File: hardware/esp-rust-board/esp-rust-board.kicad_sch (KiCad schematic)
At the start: 55 parts, among them J1 USB4105-GF-A, Q1 DMG3415U, SW1 SW_Push, SW2 SW_Push, U1 SHTC3, U2 ICM-42670-P, U3 ESP32-C3-MINI-1, U4 Rust_Board, U5 SY8088, U6 MCP73831T-2ACI/OT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

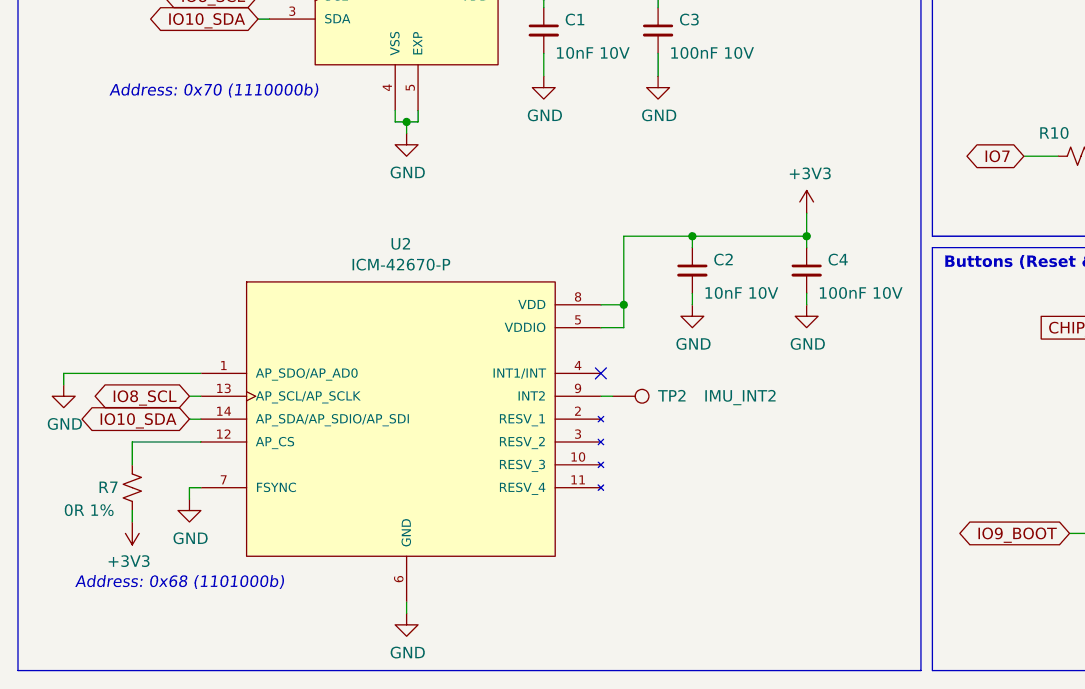
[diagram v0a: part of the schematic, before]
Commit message: Added LIS3DH
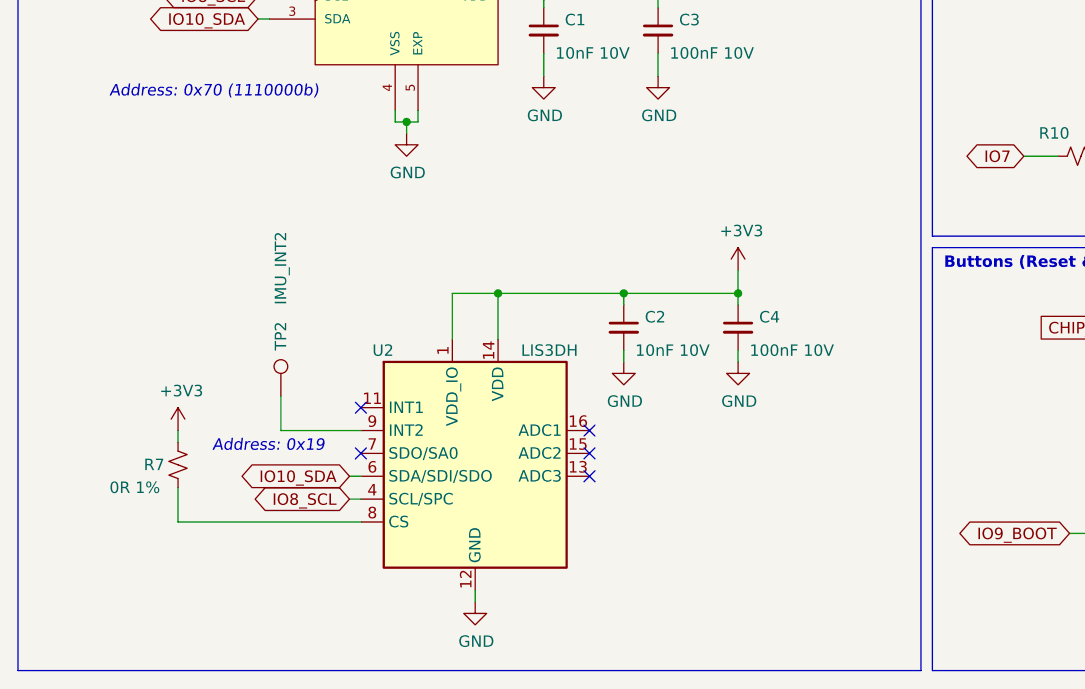
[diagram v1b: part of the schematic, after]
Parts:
- removed U2: ICM-42670-P, Rust_Board:IC_ICM-42670-P, symbol Rust_Board:ICM-42670-P
- added U2: LIS3DH, Package_LGA:LGA-16_3x3mm_P0.5mm_LayoutBorder3x5y, symbol Sensor_Motion:LIS3DH
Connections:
- net +3V3: now also R7.1, U2.1 (VDD_IO), U2.14 (VDD); no longer R7.2
- net GND: now also U2.10 (GND), U2.12 (GND), U2.5 (GND)
- net IO10_SDA: now also U2.6 (SDA/SDI/SDO)
- net IO8_SCL: now also U2.4 (SCL/SPC)
- net at TP2.1: now also U2.9 (INT2)
- new net: R7.2, U2.8 (CS)
- no-connect marks 9 -> 13
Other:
- note added: "Address: 0x19"
- note removed: "Address: 0x68 (1101000b)"
- moved on the sheet: C2, C4, R7, TP2

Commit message: Sync
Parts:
- removed TP2: IMU_INT2, TestPoint:TestPoint_Pad_D1.0mm, symbol Connector:TestPoint
- U2: LCSC (none) -> C15134
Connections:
- net +3V3: now also U2.7 (SDO/SA0)
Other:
- note added: "Address: 0x19 (0011001b)"
- note removed: "Address: 0x19"
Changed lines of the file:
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@@
   (title_block
     (title "ESP32-C3-DevKit-RUST-1")
-    (date "2022-04-27")
-    (rev "1.2a")
+    (date "2022-06-01")
+    (rev "1.2b")
     (company "Espressif")
     (comment 1 "ESP32-C3 Development Board for Rust")
+    (comment 2 "Special Version for EW22")
   )
   (junction (at 180.34 82.55) (diameter 0) (color 0 0 0 0)
@@
   )
   (no_connect (at 152.4 118.11))
+  (no_connect (at 50.8 170.18))
   (no_connect (at 231.14 81.28))
   (no_connect (at 237.49 147.32))
   (no_connect (at 237.49 139.7))
-  (no_connect (at 50.8 172.72))
   (no_connect (at 50.8 167.64))
   (no_connect (at 76.2 172.72))
@@
     (stroke (width 0) (type default) (color 0 0 0 0))
   )
-  (wire (pts (xy 41.91 170.18) (xy 50.8 170.18))
-    (stroke (width 0) (type default) (color 0 0 0 0))
-  )
   (wire (pts (xy 140.97 22.86) (xy 140.97 25.4))
     (stroke (width 0) (type default) (color 0 0 0 0))
@@
     (stroke (width 0) (type default) (color 0 0 0 0))
   )
+  (wire (pts (xy 41.91 170.18) (xy 41.91 172.72))
+    (stroke (width 0) (type default) (color 0 0 0 0))
+  )
   (wire (pts (xy 193.04 154.94) (xy 194.31 154.94))
     (stroke (width 0) (type default) (color 0 0 0 0))
@@
     (stroke (width 0) (type default) (color 0 0 0 0))
   )
-  (wire (pts (xy 41.91 166.37) (xy 41.91 170.18))
-    (stroke (width 0) (type default) (color 0 0 0 0))
-  )
   (wire (pts (xy 231.14 69.85) (xy 232.41 69.85))
     (stroke (width 0) (type default) (color 0 0 0 0))
@@
     (stroke (width 0) (type default) (color 0 0 0 0))
   )
+  (wire (pts (xy 41.91 172.72) (xy 50.8 172.72))
+    (stroke (width 0) (type default) (color 0 0 0 0))
+  )
   (wire (pts (xy 232.41 101.6) (xy 232.41 102.87))
     (stroke (width 0) (type default) (color 0 0 0 0))
@@
     (effects (font (size 1.27 1.27) (thickness 0.254) bold) (justify left bottom))
   )
-  (text "Address: 0x19" (at 34.29 172.72 0)
+  (text "Address: 0x19 (0011001b)" (at 22.86 186.69 0)
     (effects (font (size 1.27 1.27) italic) (justify left bottom))
   )
@@
     (pin "1")
   )
-  (symbol (lib_id "Connector:TestPoint") (at 41.91 166.37 0) (unit 1)
-    (in_bom no) (on_board yes)
-    (property "Reference" "TP2" (id 0) (at 41.91 161.29 90)
-      (effects (font (size 1.27 1.27)) (justify left))
-    )
-    (property "Value" "IMU_INT2" (id 1) (at 41.91 156.21 90)
-      (effects (font (size 1.27 1.27)) (justify left))
-    )
-    (property "Footprint" "TestPoint:TestPoint_Pad_D1.0mm" (id 2) (at 46.99 166.37 0)
-      (effects (font (size 1.27 1.27)) hide)
-    )
-    (property "Datasheet" "~" (id 3) (at 46.99 166.37 0)
-      (effects (font (size 1.27 1.27)) hide)
-    )
-    (pin "1")
-  )
   (symbol (lib_id "Device:C_Small") (at 80.01 158.75 0) (unit 1)
     (in_bom yes) (on_board yes)
@@
     (pin "1")
   )
+  (symbol (lib_id "power:+3V3") (at 41.91 170.18 0) (unit 1)
+    (in_bom yes) (on_board yes)
+    (property "Reference" "#PWR0112" (id 0) (at 41.91 173.99 0)
+      (effects (font (size 1.27 1.27)) hide)
+    )
+    (property "Value" "+3V3" (id 1) (at 42.291 165.7858 0))
+    (property "Footprint" "" (id 2) (at 41.91 170.18 0)
+      (effects (font (size 1.27 1.27)) hide)
+    )
+    (property "Datasheet" "" (id 3) (at 41.91 170.18 0)
+      (effects (font (size 1.27 1.27)) hide)
+    )
+    (pin "1")
+  )
   (symbol (lib_id "power:GND") (at 209.55 102.87 0) (unit 1)
     (in_bom yes) (on_board yes)
@@
       (effects (font (size 1.27 1.27)) hide)
     )
+    (property "LCSC" "C15134" (id 4) (at 63.5 172.72 0)
+      (effects (font (size 1.27 1.27)) hide)
+    )
     (pin "1")
     (pin "10")
@@
       (reference "#PWR0111") (unit 1) (value "GND") (footprint "")
     )
+    (path "/20042083-dbdf-4298-adaf-a7bd326dba79"
+      (reference "#PWR0112") (unit 1) (value "+3V3") (footprint "")
+    )
     (path "/00000000-0000-0000-0000-000061c4e20f"
       (reference "#PWR0121") (unit 1) (value "GND") (footprint "")
@@
       (reference "SW2") (unit 1) (value "SW_Push") (footprint "Button_Switch_SMD:SW_SPST_PTS810")
     )
-    (path "/00000000-0000-0000-0000-000061c2b37e"
-      (reference "TP2") (unit 1) (value "IMU_INT2") (footprint "TestPoint:TestPoint_Pad_D1.0mm")
-    )
     (path "/00000000-0000-0000-0000-000061b89283"
